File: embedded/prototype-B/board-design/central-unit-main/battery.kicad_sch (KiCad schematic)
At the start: 15 parts, among them U5 BQ24074RGT

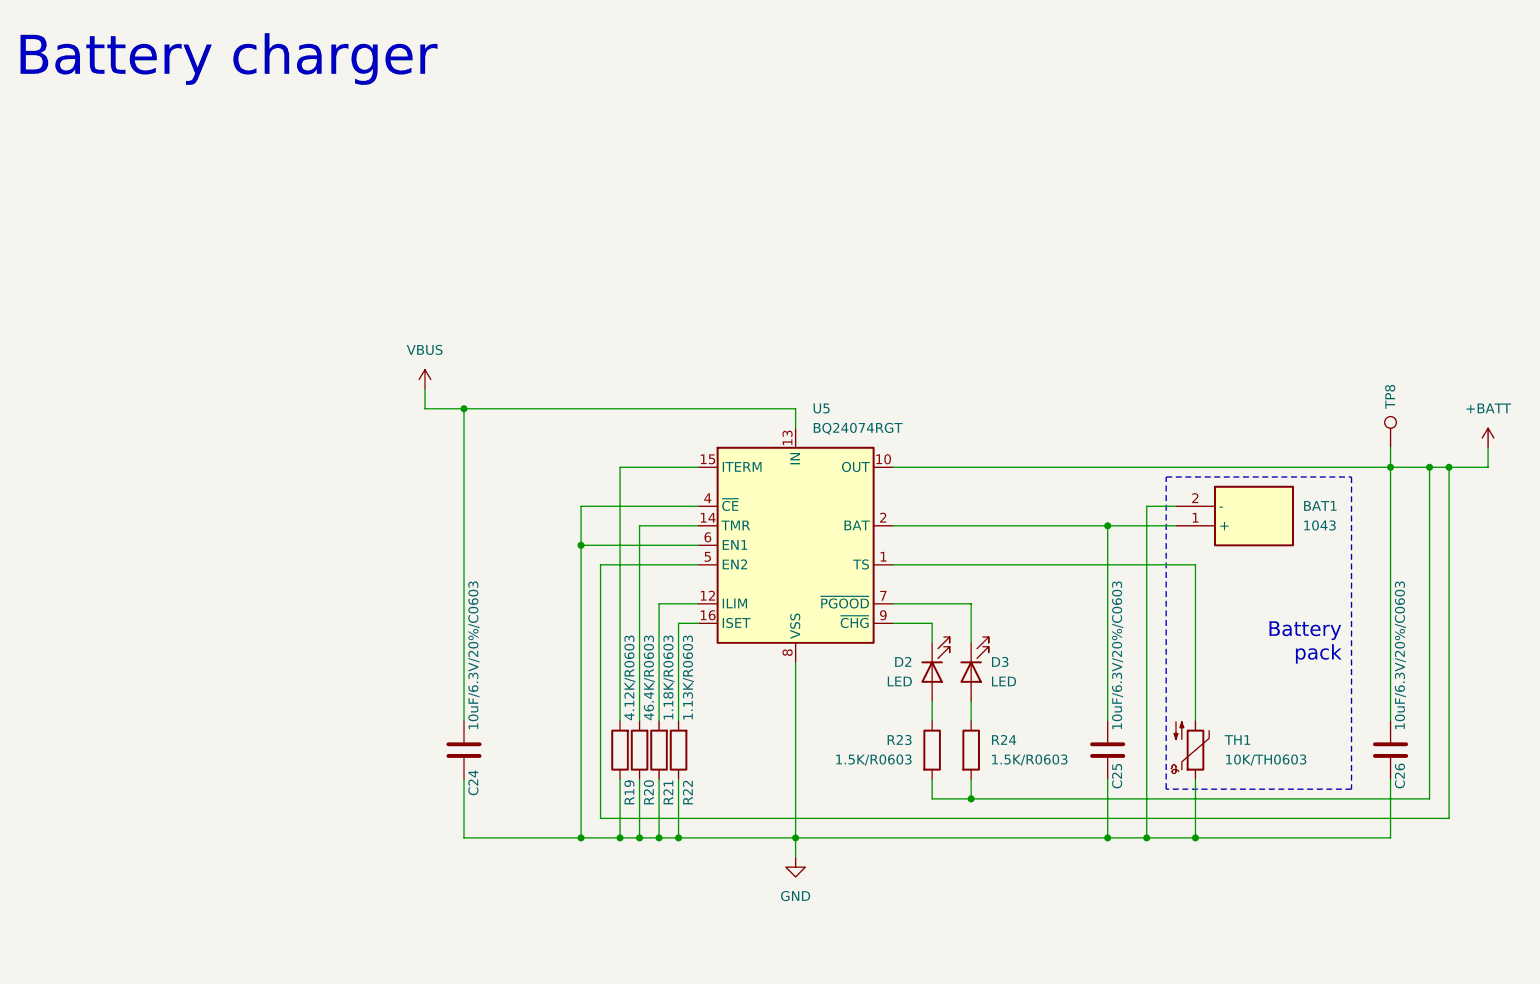
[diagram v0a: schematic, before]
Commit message: [Central unit] Change the battery charging configuration
Changed battery charger configuration to USB500. Moved voltage monitor
threshold voltage divider and power supply upstream of J1 as well.

Signed-off-by: Nicolae-Andrei Prodan <vasilenicolaeandrei@gmail.com>
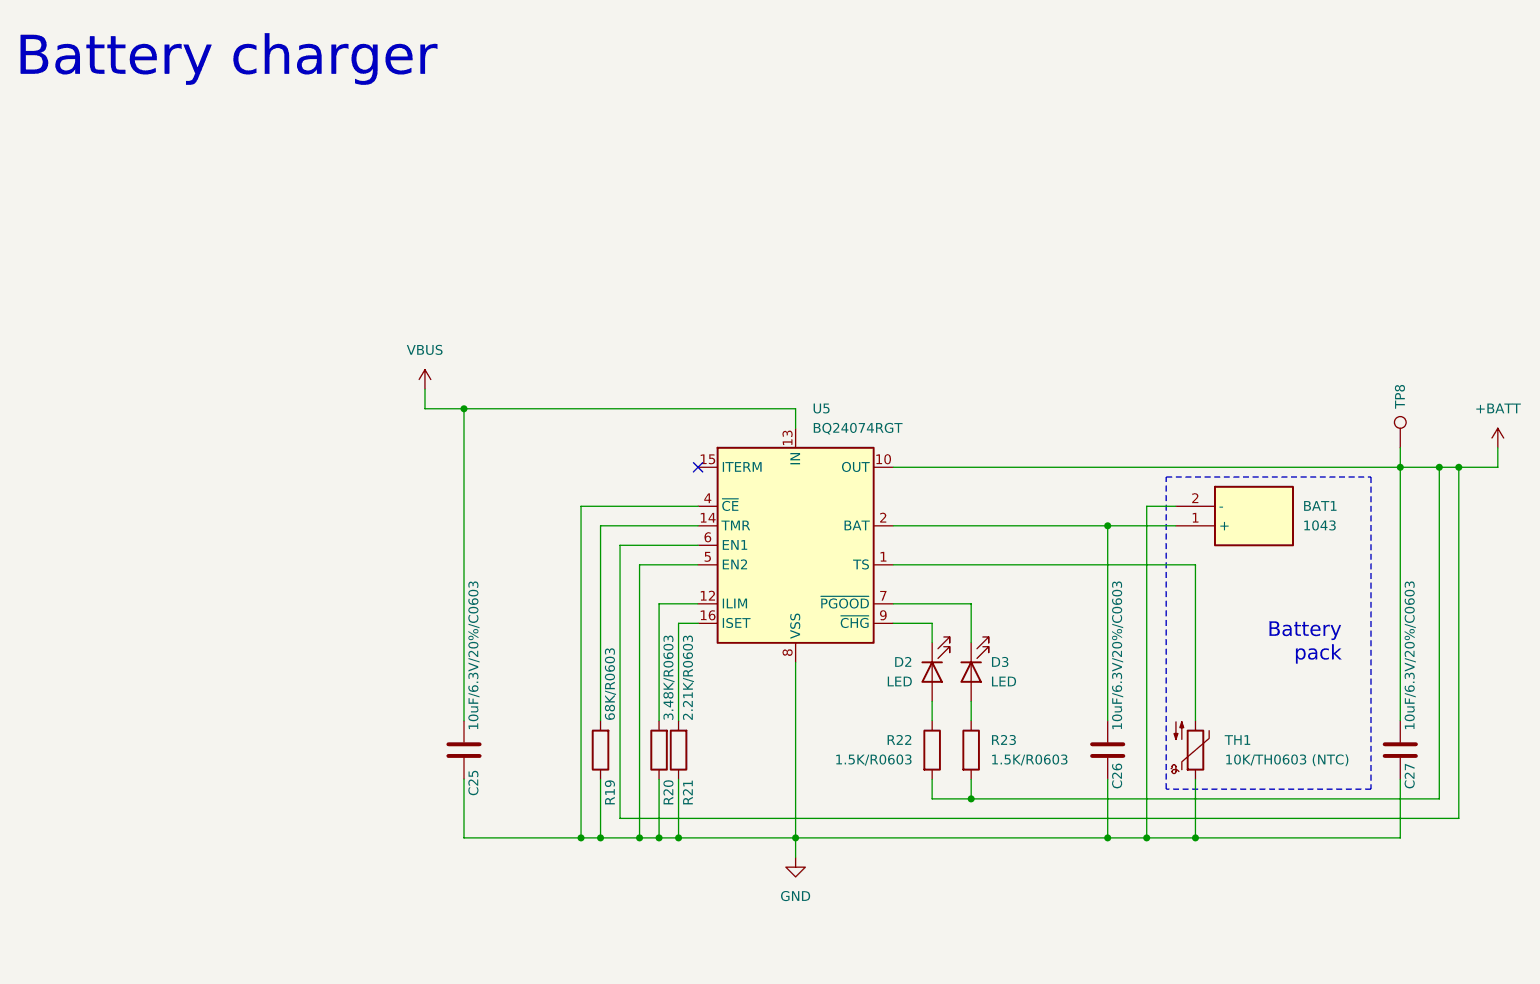
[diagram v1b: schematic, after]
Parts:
- removed R19: 4.12K/R0603, Resistor_SMD:R_0603_1608Metric_Pad0.98x0.95mm_HandSolder, symbol Device:R
- R19: renamed from R20; value 46.4K/R0603 -> 68K/R0603
- R20: renamed from R21; value 1.18K/R0603 -> 3.48K/R0603
- R21: renamed from R22; value 1.13K/R0603 -> 2.21K/R0603
- TH1: value 10K/TH0603 -> 10K/TH0603 (NTC)
- renumbered C24 to C25, C25 to C26, C26 to C27, R23 to R22, R24 to R23
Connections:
- net +BATT: now also U5.6 (EN1); no longer U5.5 (EN2)
- net GND: now also U5.5 (EN2); no longer U5.6 (EN1)
- no-connect marks 0 -> 1
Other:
- moved on the sheet: C27, R19, TP8

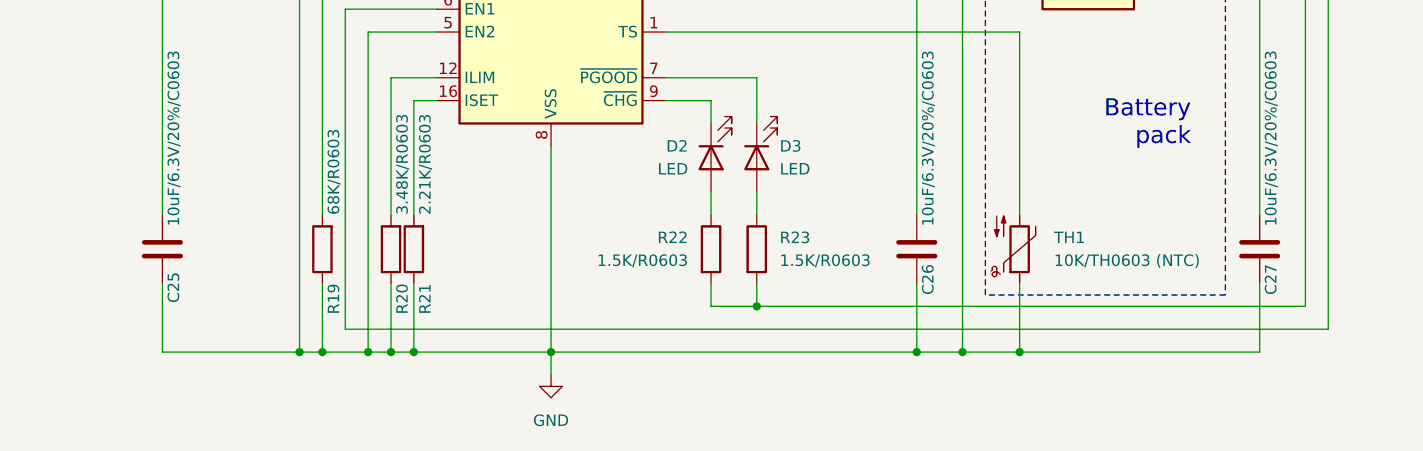
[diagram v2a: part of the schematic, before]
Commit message: [Central unit] Improve BQ24074 layout
Refactored the entire PCB layout.

Signed-off-by: Nicolae-Andrei Prodan <vasilenicolaeandrei@gmail.com>
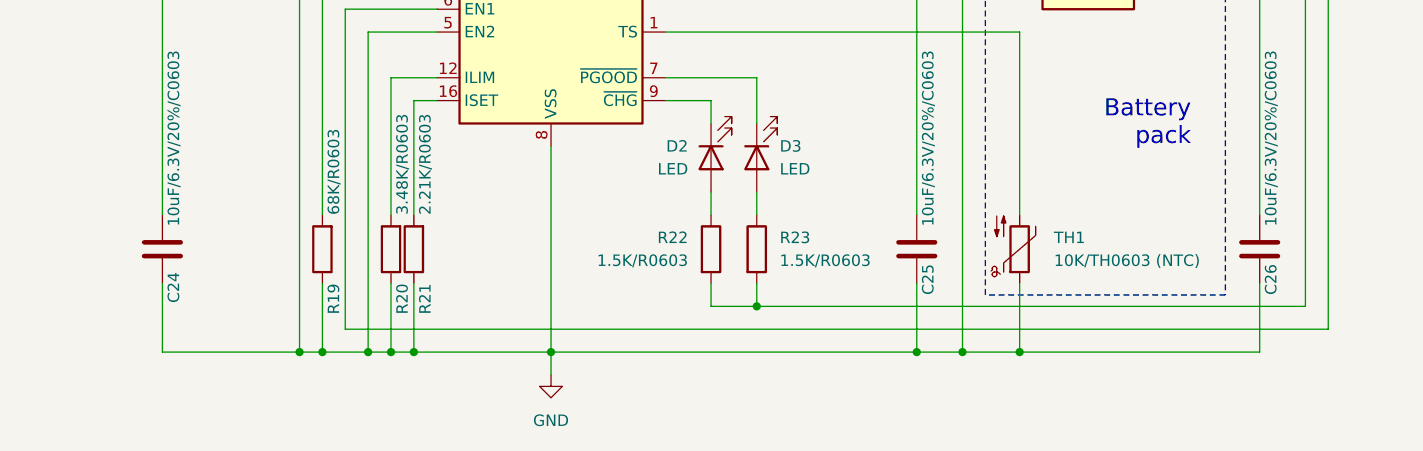
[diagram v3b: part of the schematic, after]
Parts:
- renumbered C25 to C24, C26 to C25, C27 to C26
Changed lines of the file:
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@@
 		(in_pos_files yes)
 		(dnp no)
-		(property "Reference" "C26"
+		(property "Reference" "C25"
 			(at 168.91 120.65 90)
 			(show_name no)
@@
 			(project "central-unit-main"
 				(path "/baa8ab85-8b75-4cee-ab91-40606360b161/0d9b0fcc-d01e-4009-b64e-b7ee43f093f4"
-					(reference "C26")
+					(reference "C25")
 					(unit 1)
 				)
@@
 		(in_pos_files yes)
 		(dnp no)
-		(property "Reference" "C27"
+		(property "Reference" "C26"
 			(at 207.01 120.65 90)
 			(show_name no)
@@
 			(project "central-unit-main"
 				(path "/baa8ab85-8b75-4cee-ab91-40606360b161/0d9b0fcc-d01e-4009-b64e-b7ee43f093f4"
-					(reference "C27")
+					(reference "C26")
 					(unit 1)
 				)
@@
 		(in_pos_files yes)
 		(dnp no)
-		(property "Reference" "C25"
+		(property "Reference" "C24"
 			(at 85.09 118.11 90)
 			(show_name no)
@@
 			(project "central-unit-main"
 				(path "/baa8ab85-8b75-4cee-ab91-40606360b161/0d9b0fcc-d01e-4009-b64e-b7ee43f093f4"
-					(reference "C25")
+					(reference "C24")
 					(unit 1)
 				)

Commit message: [Central unit] Redesign the power lines
Changed the battery charger footprint to a version with thermal vias.
Updated BOM.

Signed-off-by: Nicolae-Andrei Prodan <vasilenicolaeandrei@gmail.com>
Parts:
- U5: footprint Package_DFN_QFN:VQFN-16-1EP_3x3mm_P0.5mm_EP1.6x1.6mm -> Package_DFN_QFN:VQFN-16-1EP_3x3mm_P0.5mm_EP1.6x1.6mm_ThermalVias
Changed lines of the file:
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@@
 			)
 		)
-		(property "Footprint" "Package_DFN_QFN:VQFN-16-1EP_3x3mm_P0.5mm_EP1.6x1.6mm"
+		(property "Footprint" "Package_DFN_QFN:VQFN-16-1EP_3x3mm_P0.5mm_EP1.6x1.6mm_ThermalVias"
 			(at 134.62 102.87 0)
 			(hide yes)

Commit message: [All] Enhance BOM
Added the PCBWay required fields in central unit BOM for assembly
feature. Removed the jumper resistors for the crystals as well.

Signed-off-by: Nicolae-Andrei Prodan <vasilenicolaeandrei@gmail.com>
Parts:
- BAT1: MPN (none) -> 1043; Package (none) -> 1043
- C24, C25, C26: value 10uF/6.3V/20%/C0603 -> 10uF/16V/10%/C0603; MPN (none) -> CC0603KRX5R7BB106; Package (none) -> 0603 (1608 Metric)
- D2: MPN (none) -> LTST-C170KRKT; Package (none) -> 0805 (2012 Metric)
- D3: MPN (none) -> LTST-C170GKT; Package (none) -> 0805 (2012 Metric)
- R14: renamed from R19; value 68K/R0603 -> 68K/0.1W/1%/R0603; MPN (none) -> RC0603FR-0768KL; Package (none) -> 0603 (1608 Metric)
- R15: renamed from R20; value 3.48K/R0603 -> 3.48K/0.1W/1%/R0603; MPN (none) -> RC0603FR-073K48L; Package (none) -> 0603 (1608 Metric)
- R16: renamed from R21; value 2.21K/R0603 -> 2.21K/0.1W/1%/R0603; MPN (none) -> RC0603FR-072K21L; Package (none) -> 0603 (1608 Metric)
- R17: renamed from R22; value 1.5K/R0603 -> 1.5K/0.1W/1%/R0603; MPN (none) -> RC0603FR-071K5L; Package (none) -> 0603 (1608 Metric)
- R18: renamed from R23; value 1.5K/R0603 -> 1.5K/0.1W/1%/R0603; MPN (none) -> RC0603FR-071K5L; Package (none) -> 0603 (1608 Metric)
- TH1: MPN (none) -> NCU18XH103F60RB; Package (none) -> 0603 (1608 Metric)
- TP8: footprint TestPoint:TestPoint_THTPad_D2.0mm_Drill1.0mm -> TestPoint:TestPoint_Keystone_5000-5004_Miniature; MPN (none) -> 5001; Package (none) -> 5001
- U5: MPN (none) -> BQ24074RGTR; Package (none) -> 16-VQFN (3x3)

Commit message: [All] Enhance BOM
Fixed BOM issues. Added ERC and DRC reports.

Signed-off-by: Nicolae-Andrei Prodan <vasilenicolaeandrei@gmail.com>
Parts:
- D2: value LED -> LED RED
- D3: value LED -> LED GREEN
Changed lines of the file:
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@@
 			)
 		)
-		(property "Value" "LED"
+		(property "Value" "LED RED"
 			(at 142.24 106.68 90)
 			(show_name no)
@@
 			)
 		)
-		(property "Value" "LED"
+		(property "Value" "LED GREEN"
 			(at 152.4 106.68 90)
 			(show_name no)
